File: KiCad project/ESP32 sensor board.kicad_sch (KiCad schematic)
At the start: 25 parts, among them J1 USB_C_Receptacle, J2 JST_2mm_LiPo, U1 MCP73871, U2 LM1117MPX-3.3_NOPB

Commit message: Completed layout for v2.
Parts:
- J1: footprint Footprints:TE_1-2295018-2 -> Footprints:BELFUSE_SS-52400-002; symbol 1-2295018-2:1-2295018-2 -> SS-52400-002:SS-52400-002; Check_prices https://www.snapeda.com/parts/1-2295018-2/TE+Connectivity/v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 -> https://www.snapeda.com/parts/SS-52400-002/Bel+Circuit+Prot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; Description_1 USB TYPE C, REC OFFSET 0.65MM DUAL SMT -> USB Type-C Connector | USB 3.1 | 1 Port | Right Angle Recep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; MANUFACTURER TE Connectivity -> BelFuse; MAXIMUM_PACKAGE_HEIGHT 3.6 mm -> 2.96 mm; MF TE Connectivity -> Bel Fuse; MP 1-2295018-2 -> SS-52400-002; PARTREV B1 -> A0; SnapEDA_Link https://www.snapeda.com/parts/1-2295018-2/TE+Connectivity/v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 -> https://www.snapeda.com/parts/SS-52400-002/Bel+Circuit+Prot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
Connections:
- net GND: now also J1.G1 (GND/SHIELD), J1.G2 (GND/SHIELD), J1.G3 (GND/SHIELD), J1.G4 (GND/SHIELD)
- no-connect marks 10 -> 11
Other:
- moved on the sheet: C4, R3, R4

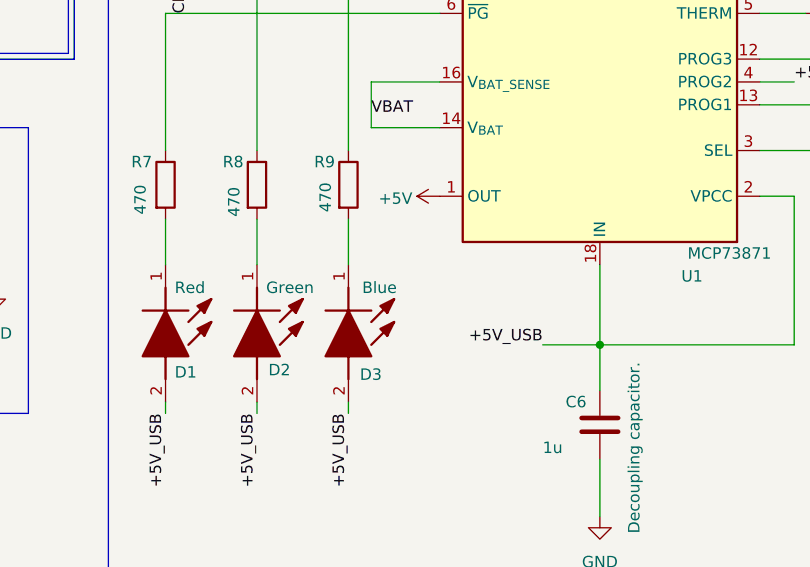
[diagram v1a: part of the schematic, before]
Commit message: Introduced new parts that can be purchased for manufacturing by NextPCB. Corrected numerous issues.
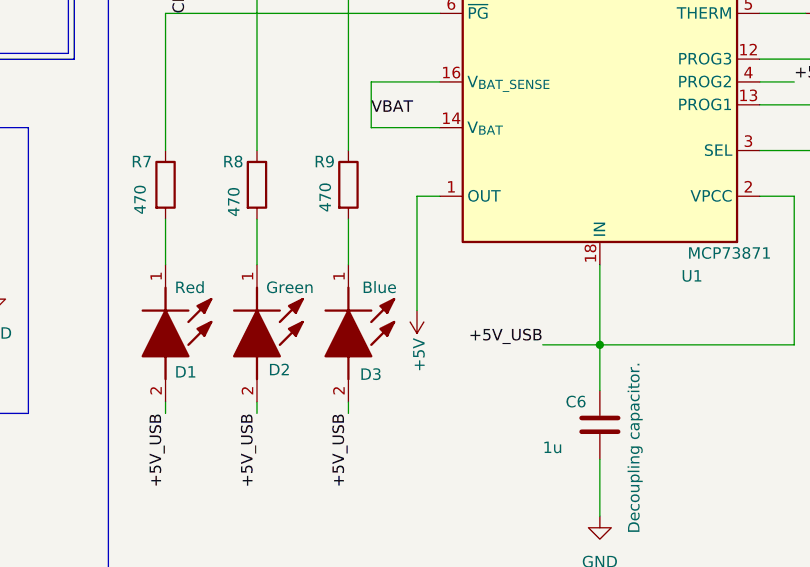
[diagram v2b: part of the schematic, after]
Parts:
- U2: footprint Footprints:VREG_LM1117MPX-3.3_NOPB -> Footprints:VREG_LM1117MPX-3.3
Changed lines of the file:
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@@
 	(wire
 		(pts
+			(xy 198.12 83.82) (xy 198.12 96.52)
+		)
+		(stroke
+			(width 0)
+			(type default)
+		)
+	)
+	(wire
+		(pts
 			(xy 69.85 54.61) (xy 74.93 54.61)
 		)
@@
 	(wire
 		(pts
+			(xy 200.66 83.82) (xy 198.12 83.82)
+		)
+		(stroke
+			(width 0)
+			(type default)
+		)
+	)
+	(wire
+		(pts
 			(xy 76.2 26.67) (xy 87.63 26.67)
 		)
@@
 	(symbol
 		(lib_id "power:+5V")
-		(at 200.66 83.82 90)
+		(at 198.12 96.52 180)
 		(unit 1)
 		(exclude_from_sim no)
@@
 		(dnp no)
 		(property "Reference" "#PWR06"
-			(at 204.47 83.82 0)
+			(at 198.12 92.71 0)
 			(effects
 				(font
@@
 		)
 		(property "Value" "+5V"
-			(at 197.612 84.074 90)
+			(at 198.374 99.568 90)
 			(effects
 				(font
@@
 		)
 		(property "Footprint" ""
-			(at 200.66 83.82 0)
+			(at 198.12 96.52 0)
 			(effects
 				(font
@@
 		)
 		(property "Datasheet" ""
-			(at 200.66 83.82 0)
+			(at 198.12 96.52 0)
 			(effects
 				(font
@@
 		)
 		(property "Description" "Power symbol creates a global label with name \"+5V\""
-			(at 200.66 83.82 0)
+			(at 198.12 96.52 0)
 			(effects
 				(font
@@
 			)
 		)
-		(property "Footprint" "Footprints:VREG_LM1117MPX-3.3_NOPB"
+		(property "Footprint" "Footprints:VREG_LM1117MPX-3.3"
 			(at 62.23 90.17 0)
 			(effects
@@
 				(hide yes)
 			)
+		)
+		(property "Comments" ""
+			(at 62.23 90.17 0)
+			(effects
+				(font
+					(size 1.27 1.27)
+				)
+				(hide yes)
+			)

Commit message: Optimisation complete.
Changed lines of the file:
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@@
 	)
 	(label "VBUS"
+		(at 137.16 156.21 0)
+		(fields_autoplaced yes)
+		(effects
+			(font
+				(size 1.27 1.27)
+			)
+			(justify left bottom)
+		)
+	)
+	(label "VBUS"
 		(at 29.21 29.21 180)
 		(fields_autoplaced yes)
@@
 		)
 	)
-	(label "+5V_USB"
-		(at 137.16 156.21 0)
-		(fields_autoplaced yes)
-		(effects
-			(font
-				(size 1.27 1.27)
-			)
-			(justify left bottom)
-		)
-	)
 	(label "USB_DN"
 		(at 137.16 143.8275 0)
@@
 		)
 		(instances
-			(project "ESP32 sensor board"
+			(project "KLP-5e-ESP32-sensor-board-2.1_modifications"
 				(path "/16c571a0-8550-4f05-972c-22b0701cbf02"
 					(page "2")

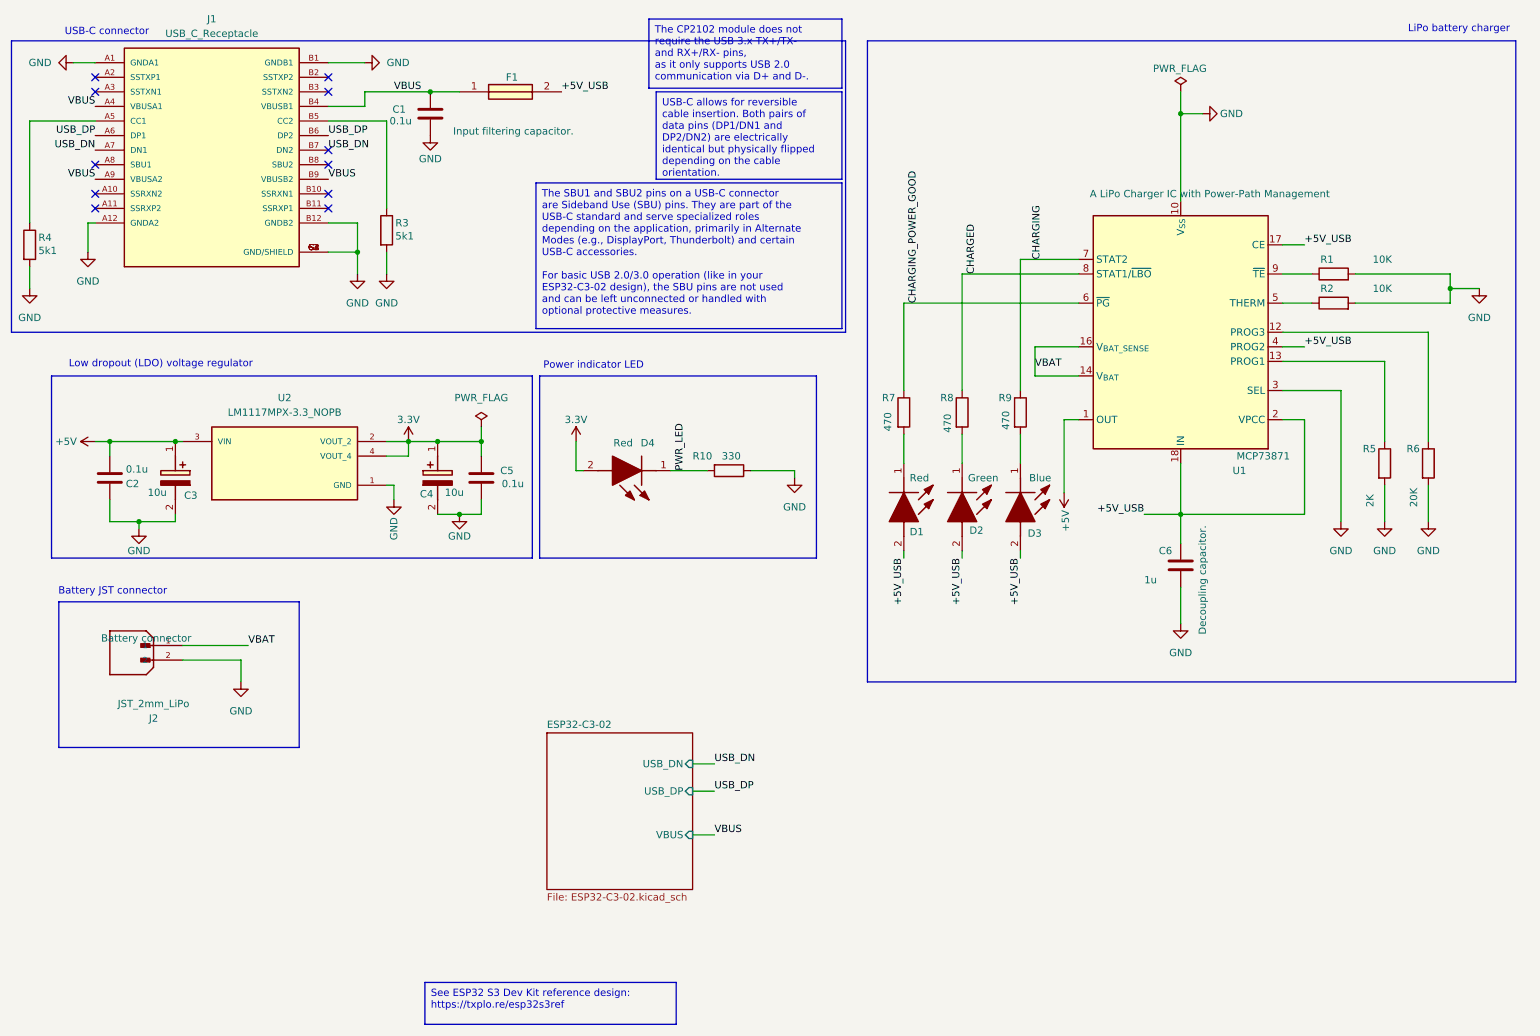
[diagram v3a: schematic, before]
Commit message: Fixed and improved Schematic design:
* Changed the buttons
* Added a ferrite bead at the output of the charger to cut some possible noise.
* Changed the values of R30, R31 and C19, and i add a 100K trimmer to set the gain from 25x to 125x.
* Added C23, C24 and C25 in the photo sensor circuit
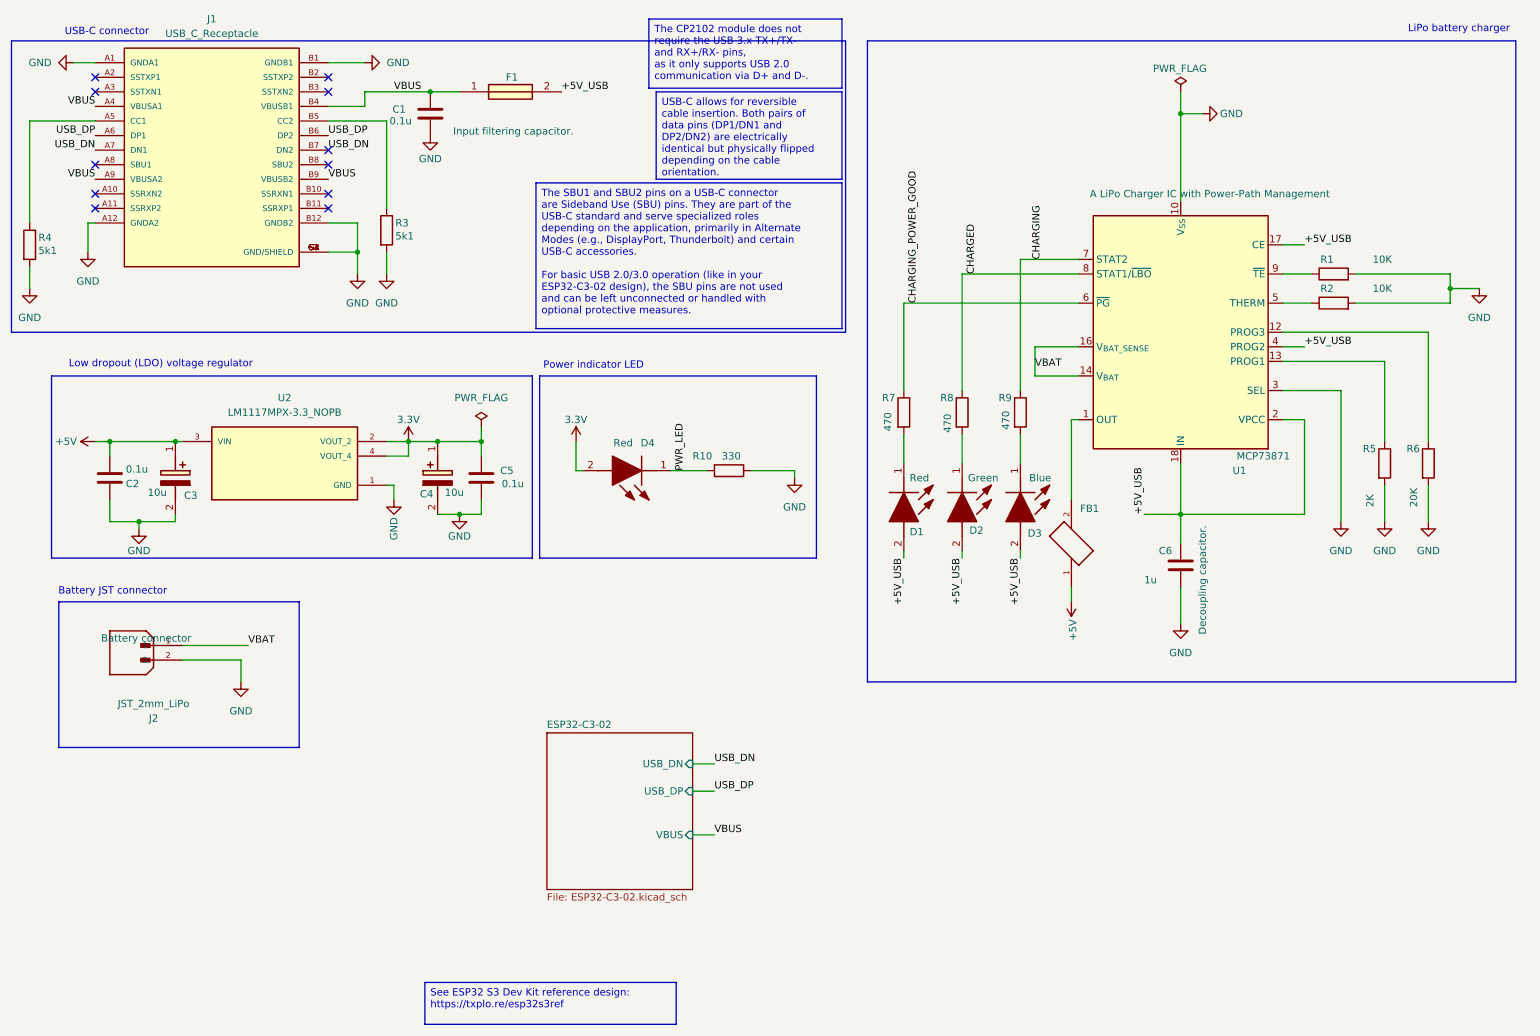
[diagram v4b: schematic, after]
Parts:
- added FB1: FBMJ2125HM330-T, FBMJ2125HM330-T:BEADC2012X105N, symbol FBMJ2125HM330-T:FBMJ2125HM330-T
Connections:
- net +5V: now also FB1.1; no longer U1.1 (OUT), U1.20 (OUT)
- new net: FB1.2, U1.1 (OUT), U1.20 (OUT)

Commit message: Completed symbol-footprint associations.
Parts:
- FB1: footprint FBMJ2125HM330-T:BEADC2012X105N -> Footprints:BEADC2012X105N
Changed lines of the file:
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@@
 			)
 		)
-		(property "Footprint" "FBMJ2125HM330-T:BEADC2012X105N"
+		(property "Footprint" "Footprints:BEADC2012X105N"
 			(at 199.39 105.41 0)
 			(effects
